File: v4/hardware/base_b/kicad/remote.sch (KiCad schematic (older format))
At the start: 33 parts, among them J1 Conn_Coaxial, J16 Conn_01x04_Female, J19 Conn_01x03_Female, J2 Conn_01x06_Female, J20 Conn_01x04_Female, J3 Conn_01x04_Female, J5 Conn_01x03_Female, Q1 Q_NMOS_GDS, Q3 Q_NPN_EBC, SW1 SW_Push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

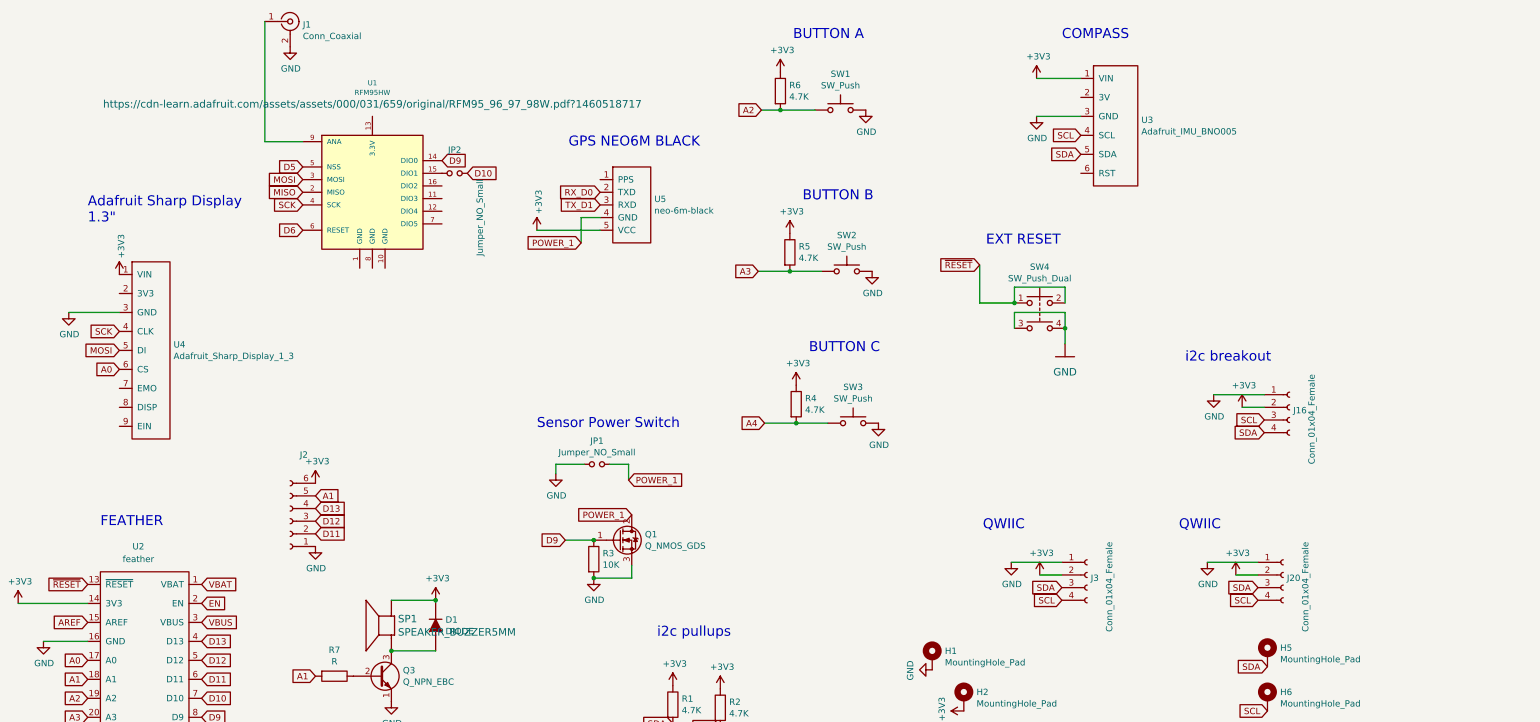
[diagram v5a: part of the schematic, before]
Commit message: routed power lines
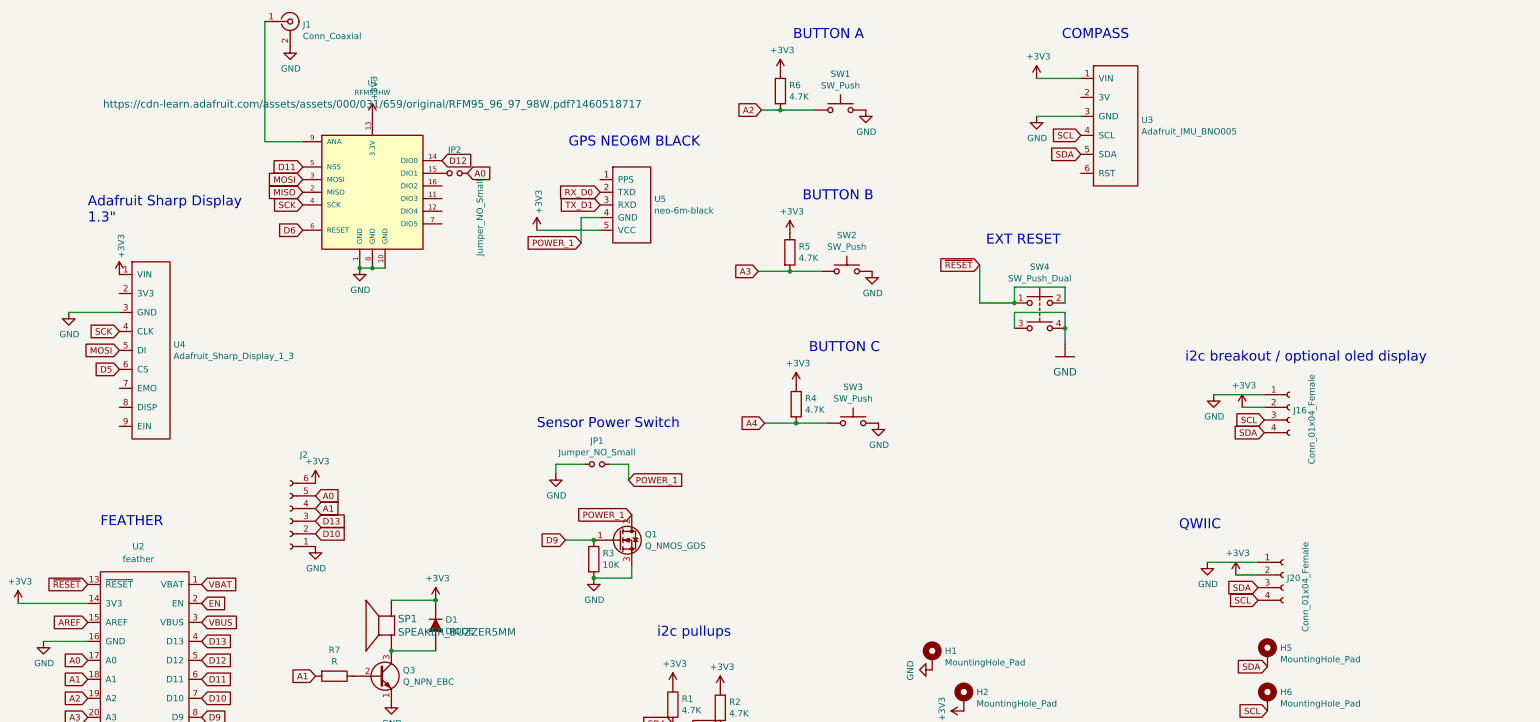
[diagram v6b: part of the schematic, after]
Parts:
- removed J3: Conn_01x04_Female, Connector_JST:JST_SH_SM04B-SRSS-TB_1x04-1MP_P1.00mm_Horizontal, symbol Connector:Conn_01x04_Female
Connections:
- net +3V3: now also U1.13 (3.3V)
- net A0: now also J2.5 (Pin_5), JP2.2; no longer U4.6 (CS)
- net A1: now also J2.4 (Pin_4); no longer J2.5 (Pin_5)
- net D10: now also J2.2 (Pin_2); no longer JP2.2
- net D11: now also U1.5 (NSS); no longer J2.2 (Pin_2)
- net D12: now also U1.14 (DIO0); no longer J2.3 (Pin_3)
- net D13: now also J2.3 (Pin_3); no longer J2.4 (Pin_4)
- net D5: now also U4.6 (CS); no longer U1.5 (NSS)
- net D9: no longer U1.14 (DIO0)
- net GND: now also U1.1 (GND), U1.10 (GND), U1.8 (GND)
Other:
- note added: "i2c breakout / optional oled display"
- note removed: "i2c breakout"
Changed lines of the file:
@@
 	1    0    0    -1
 $EndComp
-Text Notes 9775 3450 0    79   ~ 0
-i2c breakout
 $Comp
 L Mechanical:MountingHole_Pad H1
@@
 	5100 4850 4875 4850
 Connection ~ 5100 4850
-Text GLabel 1350 3500 0    50   Input ~ 0
+Text GLabel 2900 4500 2    50   Input ~ 0
 A0
 Text GLabel 1350 3350 0    50   Input ~ 0
@@
 Text GLabel 2000 6400 2    50   Input ~ 0
 D6
-Text GLabel 2800 1900 0    50   Input ~ 0
+Text GLabel 1350 3500 0    50   Input ~ 0
 D5
 Text GLabel 2800 2400 0    50   Input ~ 0
 D6
 Text GLabel 3900 1850 2    50   Input ~ 0
-D9
+D12
 Text GLabel 2000 6100 2    50   Input ~ 0
 D10
@@
 Wire Wire Line
 	550  5350 1100 5350
-$Comp
-L device:Jumper_NO_Small JP2
-U 1 1 61E9417E
-P 4000 1950
-F 0 "JP2" H 4000 2135 50  0000 C CNN
-F 1 "Jumper_NO_Small" V 4200 1600 50  0000 C CNN
-F 2 "Jumper:SolderJumper-2_P1.3mm_Open_Pad1.0x1.5mm" H 4000 1950 50  0001 C CNN
-F 3 "" H 4000 1950 50  0001 C CNN
-	1    4000 1950
-	1    0    0    -1
-$EndComp
-Text GLabel 4100 1950 2    50   Input ~ 0
-D10
-Text GLabel 2900 4600 2    50   Input ~ 0
+Text GLabel 2900 4700 2    50   Input ~ 0
 D13
-Text GLabel 2900 4700 2    50   Input ~ 0
-D12
-Text GLabel 2900 4800 2    50   Input ~ 0
+Text GLabel 2800 1900 0    50   Input ~ 0
 D11
-Text GLabel 2900 4500 2    50   Input ~ 0
-A1
 $Comp
 L power:+3V3 #PWR0117
@@
 	-1   0    0    1
 $EndComp
-Text Notes 8175 4775 0    79   ~ 0
-QWIIC
-$Comp
-L Connector:Conn_01x04_Female J3
-U 1 1 61F816B3
-P 9000 5125
-F 0 "J3" H 9028 5101 50  0000 L CNN
-F 1 "Conn_01x04_Female" V 9175 4675 50  0000 L CNN
-F 2 "Connector_JST:JST_SH_SM04B-SRSS-TB_1x04-1MP_P1.00mm_Horizontal" H 9000 5125 50  0001 C CNN
-F 3 "~" H 9000 5125 50  0001 C CNN
-	1    9000 5125
-	1    0    0    -1
-$EndComp
-Wire Wire Line
-	8800 5125 8625 5125
-Wire Wire Line
-	8800 5025 8400 5025
-Text GLabel 8800 5325 0    50   Input ~ 0
-SCL
-Text GLabel 8800 5225 0    50   Input ~ 0
-SDA
-$Comp
-L power:+3V3 #PWR0120
-U 1 1 61F816C1
-P 8625 5125
-F 0 "#PWR0120" H 8625 4975 50  0001 C CNN
-F 1 "+3V3" H 8640 5298 50  0000 C CNN
-F 2 "" H 8625 5125 50  0001 C CNN
-F 3 "" H 8625 5125 50  0001 C CNN
-	1    8625 5125
-	1    0    0    -1
-$EndComp
-$Comp
-L power:GND #PWR0121
-U 1 1 61F816CB
-P 8400 5025
-F 0 "#PWR0121" H 8400 4775 50  0001 C CNN
-F 1 "GND" H 8405 4852 50  0000 C CNN
-F 2 "" H 8400 5025 50  0001 C CNN
-F 3 "" H 8400 5025 50  0001 C CNN
-	1    8400 5025
-	1    0    0    -1
-$EndComp
 $Comp
 L power:GND #PWR0122
@@
 Wire Wire Line
 	4350 7100 3950 7100
+$Comp
+L power:GND #PWR0124
+U 1 1 6207EF12
+P 3250 2700
+F 0 "#PWR0124" H 3250 2450 50  0001 C CNN
+F 1 "GND" H 3255 2527 50  0000 C CNN
+F 2 "" H 3250 2700 50  0001 C CNN
+F 3 "" H 3250 2700 50  0001 C CNN
+	1    3250 2700
+	1    0    0    -1
+$EndComp
+Wire Wire Line
+	3250 2700 3350 2700
+Connection ~ 3250 2700
+Wire Wire Line
+	3350 2700 3450 2700
+Connection ~ 3350 2700
+$Comp
+L device:Jumper_NO_Small JP2
+U 1 1 61E9417E
+P 4000 1950
+F 0 "JP2" H 4000 2135 50  0000 C CNN
+F 1 "Jumper_NO_Small" V 4200 1600 50  0000 C CNN
+F 2 "Jumper:SolderJumper-2_P1.3mm_Open_Pad1.0x1.5mm" H 4000 1950 50  0001 C CNN
+F 3 "" H 4000 1950 50  0001 C CNN
+	1    4000 1950
+	1    0    0    -1
+$EndComp
+Text GLabel 2900 4800 2    50   Input ~ 0
+D10
+Text GLabel 2900 4600 2    50   Input ~ 0
+A1
+Text GLabel 4100 1950 2    50   Input ~ 0
+A0
+Text Notes 9775 3450 0    79   ~ 0
+i2c breakout / optional oled display
+$Comp
+L power:+3V3 #PWR?
+U 1 1 6216FD88
+P 3350 1500
+F 0 "#PWR?" H 3350 1350 50  0001 C CNN
+F 1 "+3V3" V 3365 1628 50  0000 L CNN
+F 2 "" H 3350 1500 50  0001 C CNN
+F 3 "" H 3350 1500 50  0001 C CNN
+	1    3350 1500
+	1    0    0    -1
+$EndComp
 $EndSCHEMATC
